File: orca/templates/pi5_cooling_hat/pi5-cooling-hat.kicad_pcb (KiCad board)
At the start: 2 copper layers, 65 x 56.5 mm, 19 parts, among them J1 Raspberry Pi 5 GPIO, J2 5V 4-wire PWM fan, Q1 2N7000

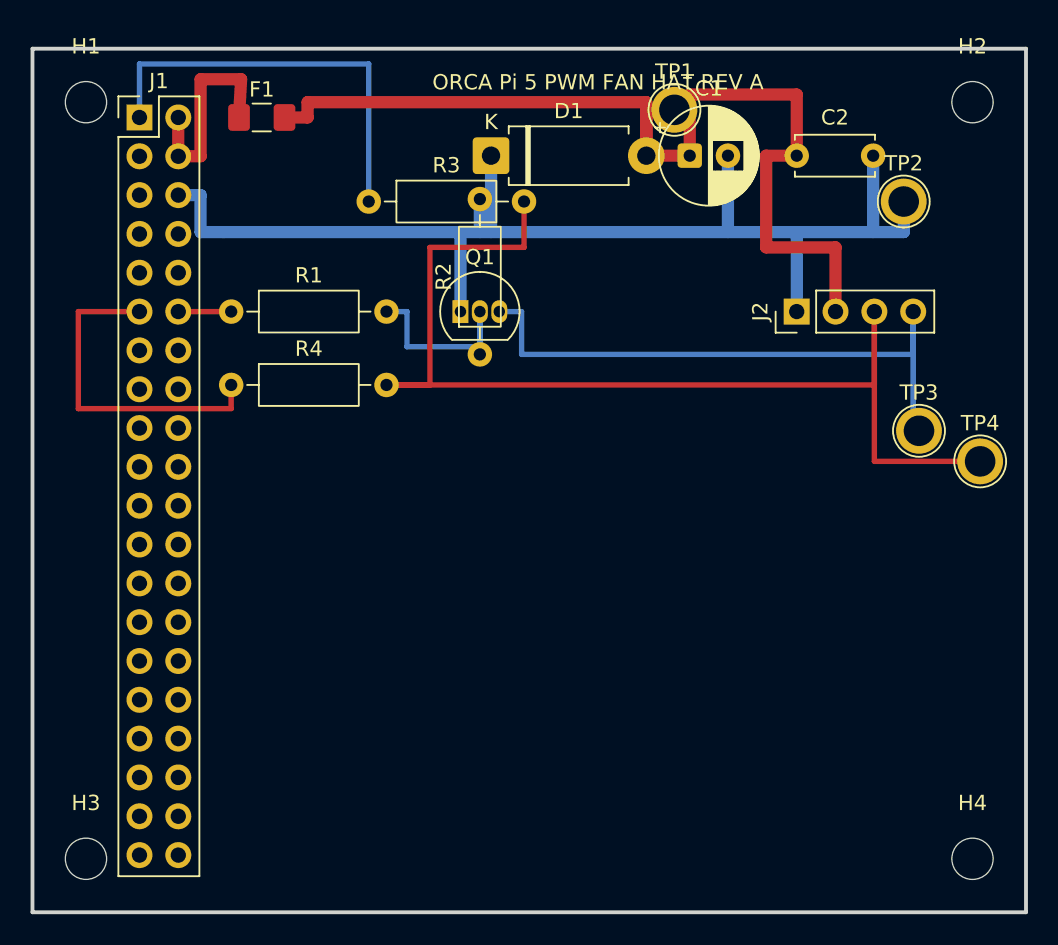
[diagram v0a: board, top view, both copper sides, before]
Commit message: Add free engineering review panel and repair Pi HAT design
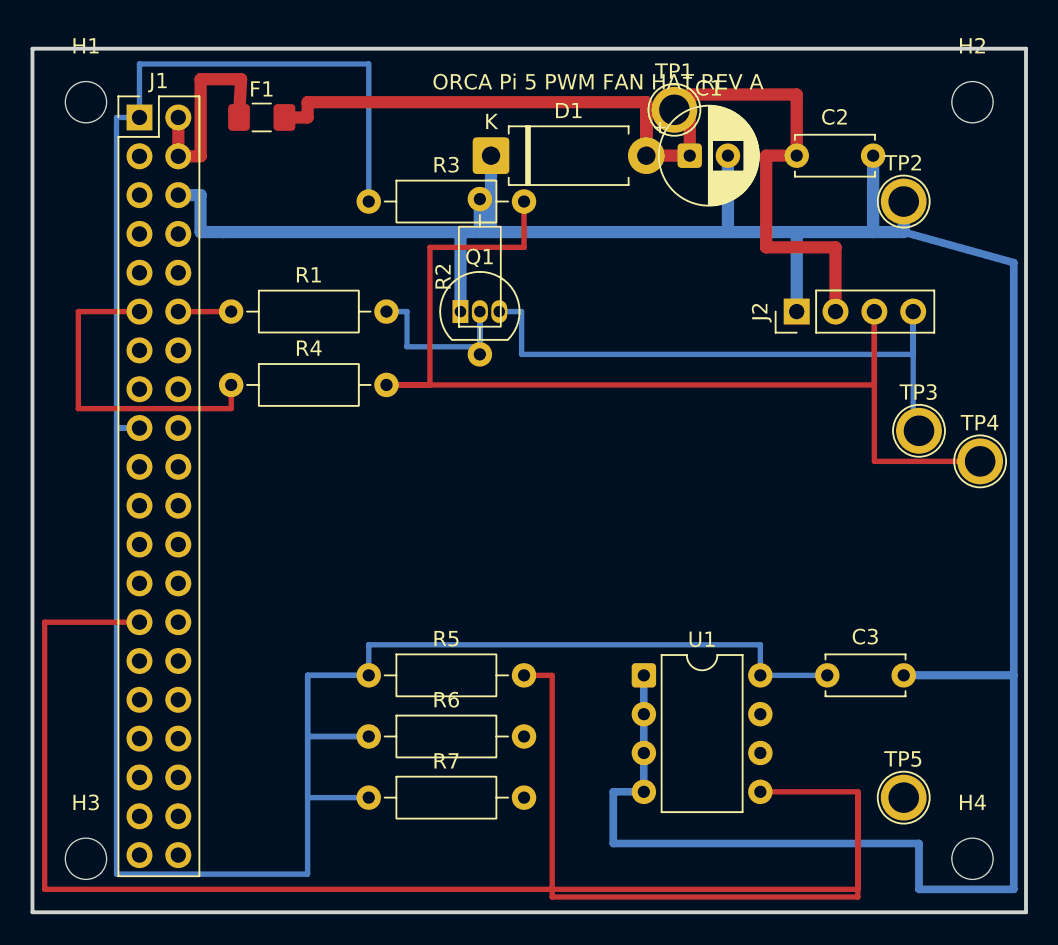
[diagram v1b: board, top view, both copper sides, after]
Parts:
- added C3: 100nF, C_Disc_D5.0mm_W2.5mm_P5.00mm, F.Cu at (72.0, 61.0)
- added R5: 3.9k, R_Axial_DIN0207_L6.3mm_D2.5mm_P10.16mm_Horizontal, F.Cu at (42.0, 61.0)
- added R6: 3.9k, R_Axial_DIN0207_L6.3mm_D2.5mm_P10.16mm_Horizontal, F.Cu at (42.0, 65.0)
- added R7: 1k, R_Axial_DIN0207_L6.3mm_D2.5mm_P10.16mm_Horizontal, F.Cu at (42.0, 69.0)
- added TP5: EEPROM_WP, TestPoint_Plated_Hole_D2.0mm, F.Cu at (77.0, 69.0)
- added U1: CAT24C32, DIP-8_W7.62mm, F.Cu at (60.0, 61.0)
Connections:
- J1 pad 17: (no net) -> 3V3
- J1 pad 27: (no net) -> ID_SD
- J1 pad 28: (no net) -> ID_SC
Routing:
- net 3V3: track 27.5 -> 169.0 mm
- net ID_SD: track 0.00 -> 132.9 mm
- net GND: track 79.4 -> 186.5 mm
- net ID_SC: track 0.00 -> 77.1 mm
- net EEPROM_WP: track 0.00 -> 49.7 mm
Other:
- copper layers 2 -> 4
